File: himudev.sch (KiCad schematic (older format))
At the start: 2 parts

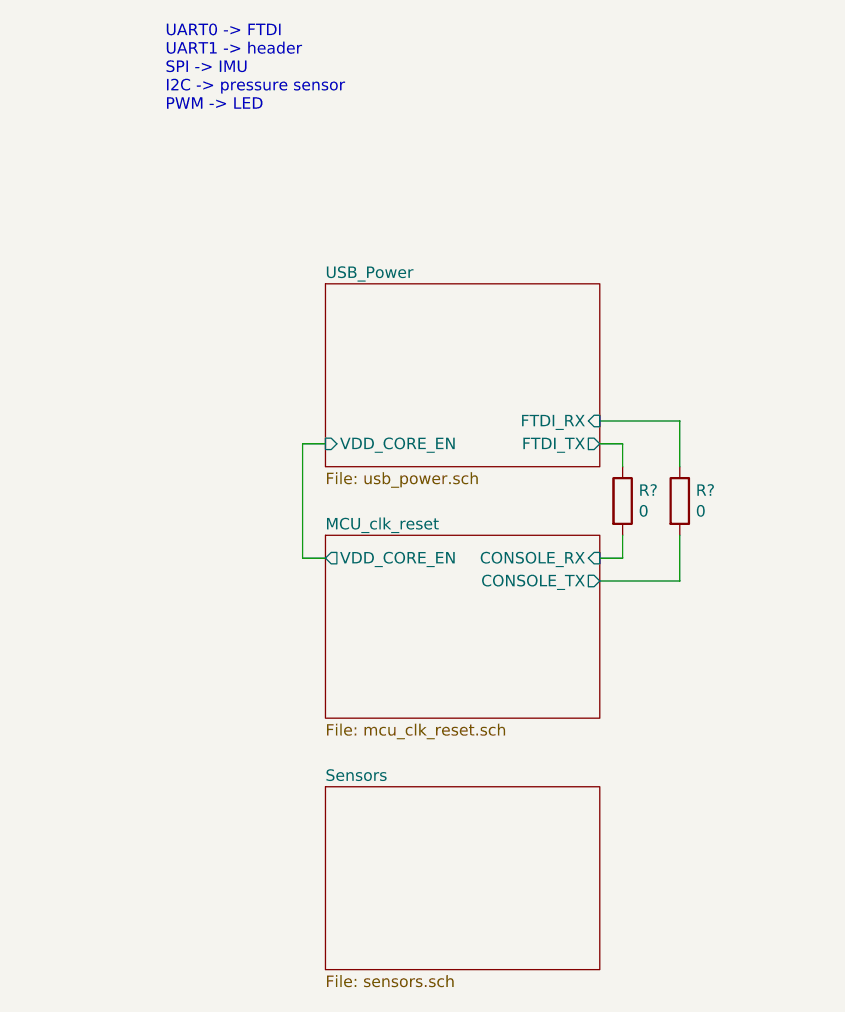
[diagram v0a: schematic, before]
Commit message: First full version of a schematic
This commit is a quicksave of completed but not reviewed schematic.
Added pressure sensor, finished IMU wiring, finished top-level
schematic, added pin header, placed LEDs and many others.
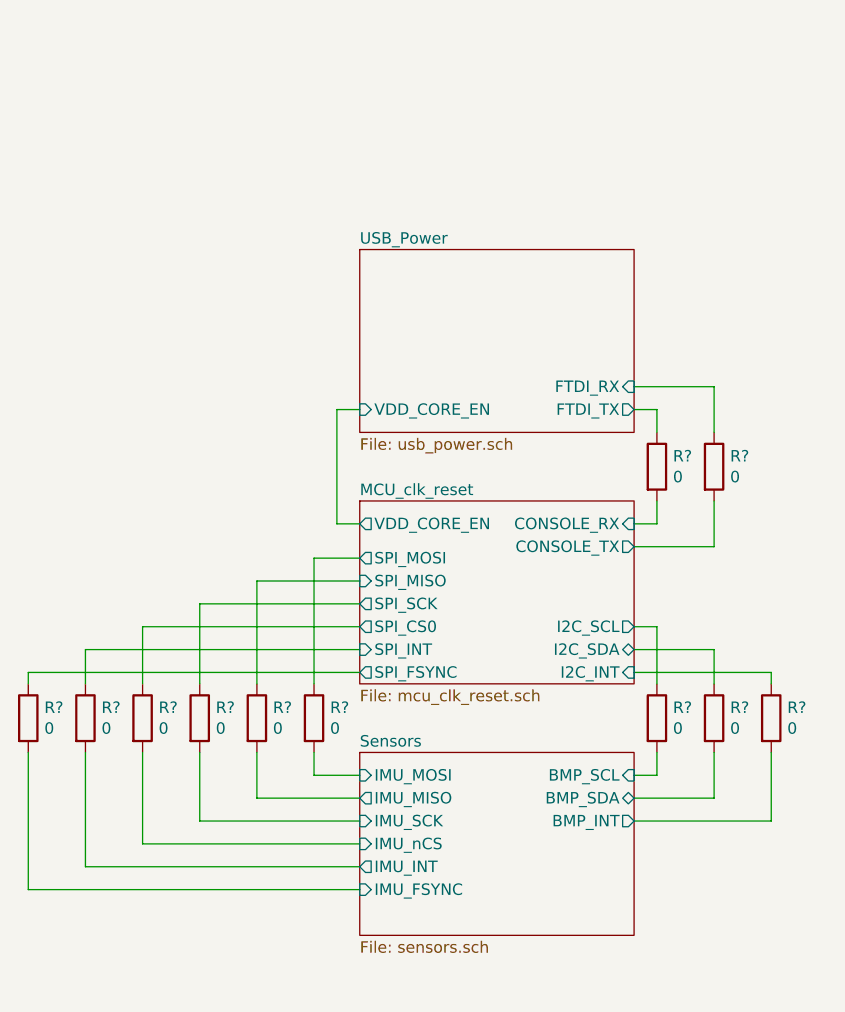
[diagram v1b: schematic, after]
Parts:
- added R? (x9): 0, symbol Device:R
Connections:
- new net MCU_clk_reset/I2C_INT: R?.1
- new net MCU_clk_reset/I2C_SCL: R?.1
- new net MCU_clk_reset/I2C_SDA: R?.1
- new net MCU_clk_reset/SPI_CS0: R?.1
- new net MCU_clk_reset/SPI_FSYNC: R?.1
- new net MCU_clk_reset/SPI_INT: R?.1
- new net MCU_clk_reset/SPI_MISO: R?.1
- new net MCU_clk_reset/SPI_MOSI: R?.1
- new net MCU_clk_reset/SPI_SCK: R?.1
- new net Sensors/BMP_INT: R?.2
- new net Sensors/BMP_SCL: R?.2
- new net Sensors/BMP_SDA: R?.2
- new net Sensors/IMU_FSYNC: R?.2
- new net Sensors/IMU_INT: R?.2
- new net Sensors/IMU_MISO: R?.2
- new net Sensors/IMU_MOSI: R?.2
- new net Sensors/IMU_SCK: R?.2
- new net Sensors/IMU_nCS: R?.2
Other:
- note removed: "UART0 -> FTDI\nUART1 -> header\nSPI -> IMU\nI2C -> pressure sensor\nPWM -> LED"
- moved on the sheet: R?

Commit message: Add ERC fixes, mostly PWR_FLAGs
Also, fixed MCP1726 symbol.
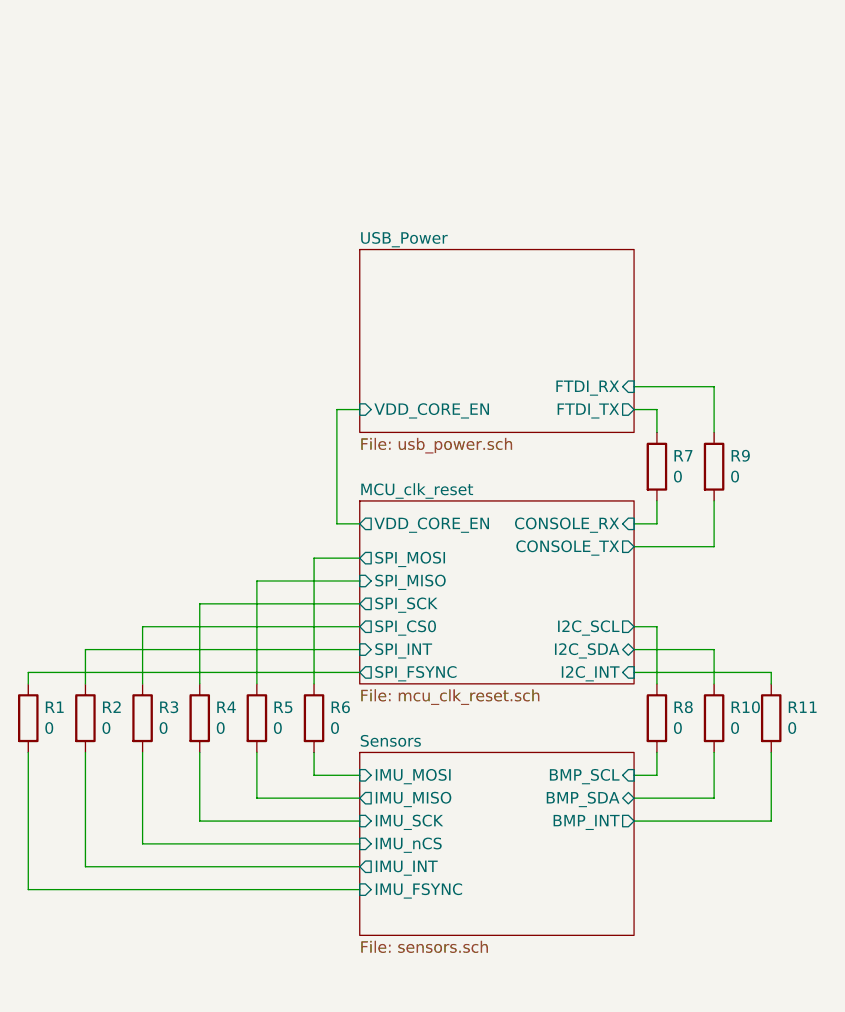
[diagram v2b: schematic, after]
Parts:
- gave numbers to parts that had none: 11
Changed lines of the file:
@@
 	6550 3650 6450 3650
 $Comp
-L Device:R R?
+L Device:R R7
 U 1 1 5E01A1E6
 P 6550 3400
-F 0 "R?" H 6620 3446 50  0000 L CNN
+F 0 "R7" H 6620 3446 50  0000 L CNN
 F 1 "0" H 6620 3355 50  0000 L CNN
 F 2 "" V 6480 3400 50  0001 C CNN
@@
 $EndComp
 $Comp
-L Device:R R?
+L Device:R R9
 U 1 1 5E01A80B
 P 6800 3400
-F 0 "R?" H 6870 3446 50  0000 L CNN
+F 0 "R9" H 6870 3446 50  0000 L CNN
 F 1 "0" H 6870 3355 50  0000 L CNN
 F 2 "" V 6730 3400 50  0001 C CNN
@@
 	6550 4750 6450 4750
 $Comp
-L Device:R R?
+L Device:R R8
 U 1 1 5EC7E790
 P 6550 4500
-F 0 "R?" H 6620 4546 50  0000 L CNN
+F 0 "R8" H 6620 4546 50  0000 L CNN
 F 1 "0" H 6620 4455 50  0000 L CNN
 F 2 "" V 6480 4500 50  0001 C CNN
@@
 $EndComp
 $Comp
-L Device:R R?
+L Device:R R10
 U 1 1 5EC7E796
 P 6800 4500
-F 0 "R?" H 6870 4546 50  0000 L CNN
+F 0 "R10" H 6870 4546 50  0000 L CNN
 F 1 "0" H 6870 4455 50  0000 L CNN
 F 2 "" V 6730 4500 50  0001 C CNN
@@
 	6450 4850 6800 4850
 $Comp
-L Device:R R?
+L Device:R R11
 U 1 1 5EC7F0AC
 P 7050 4500
-F 0 "R?" H 7120 4546 50  0000 L CNN
+F 0 "R11" H 7120 4546 50  0000 L CNN
 F 1 "0" H 7120 4455 50  0000 L CNN
 F 2 "" V 6980 4500 50  0001 C CNN
@@
 	6450 4950 7050 4950
 $Comp
-L Device:R R?
+L Device:R R4
 U 1 1 5ECADCAC
 P 4550 4500
-F 0 "R?" H 4620 4546 50  0000 L CNN
+F 0 "R4" H 4620 4546 50  0000 L CNN
 F 1 "0" H 4620 4455 50  0000 L CNN
 F 2 "" V 4480 4500 50  0001 C CNN
@@
 $EndComp
 $Comp
-L Device:R R?
+L Device:R R5
 U 1 1 5ECADCB2
 P 4800 4500
-F 0 "R?" H 4870 4546 50  0000 L CNN
+F 0 "R5" H 4870 4546 50  0000 L CNN
 F 1 "0" H 4870 4455 50  0000 L CNN
 F 2 "" V 4730 4500 50  0001 C CNN
@@
 $EndComp
 $Comp
-L Device:R R?
+L Device:R R6
 U 1 1 5ECADCB8
 P 5050 4500
-F 0 "R?" H 5120 4546 50  0000 L CNN
+F 0 "R6" H 5120 4546 50  0000 L CNN
 F 1 "0" H 5120 4455 50  0000 L CNN
 F 2 "" V 4980 4500 50  0001 C CNN
@@
 $EndComp
 $Comp
-L Device:R R?
+L Device:R R1
 U 1 1 5ECAE892
 P 3800 4500
-F 0 "R?" H 3870 4546 50  0000 L CNN
+F 0 "R1" H 3870 4546 50  0000 L CNN
 F 1 "0" H 3870 4455 50  0000 L CNN
 F 2 "" V 3730 4500 50  0001 C CNN
@@
 $EndComp
 $Comp
-L Device:R R?
+L Device:R R2
 U 1 1 5ECAE898
 P 4050 4500
-F 0 "R?" H 4120 4546 50  0000 L CNN
+F 0 "R2" H 4120 4546 50  0000 L CNN
 F 1 "0" H 4120 4455 50  0000 L CNN
 F 2 "" V 3980 4500 50  0001 C CNN
@@
 $EndComp
 $Comp
-L Device:R R?
+L Device:R R3
 U 1 1 5ECAE89E
 P 4300 4500
-F 0 "R?" H 4370 4546 50  0000 L CNN
+F 0 "R3" H 4370 4546 50  0000 L CNN
 F 1 "0" H 4370 4455 50  0000 L CNN
 F 2 "" V 4230 4500 50  0001 C CNN

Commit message: Assigned footprints, generated netlist
I can already see some footprints issues. Eg. the switches have to be
changed to the SMT version. There are some silkscreen issues in custom
oscillator footprints. Otherwise looks promising :)
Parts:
- R1, R10, R11, R2, R3, R4, R5, R6, R7, R8, R9: footprint (none) -> Resistor_SMD:R_0805_2012Metric_Pad1.15x1.40mm_HandSolder
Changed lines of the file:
@@
 F 0 "R7" H 6620 3446 50  0000 L CNN
 F 1 "0" H 6620 3355 50  0000 L CNN
-F 2 "" V 6480 3400 50  0001 C CNN
+F 2 "Resistor_SMD:R_0805_2012Metric_Pad1.15x1.40mm_HandSolder" V 6480 3400 50  0001 C CNN
 F 3 "~" H 6550 3400 50  0001 C CNN
 	1    6550 3400
@@
 F 0 "R9" H 6870 3446 50  0000 L CNN
 F 1 "0" H 6870 3355 50  0000 L CNN
-F 2 "" V 6730 3400 50  0001 C CNN
+F 2 "Resistor_SMD:R_0805_2012Metric_Pad1.15x1.40mm_HandSolder" V 6730 3400 50  0001 C CNN
 F 3 "~" H 6800 3400 50  0001 C CNN
 	1    6800 3400
@@
 F 0 "R8" H 6620 4546 50  0000 L CNN
 F 1 "0" H 6620 4455 50  0000 L CNN
-F 2 "" V 6480 4500 50  0001 C CNN
+F 2 "Resistor_SMD:R_0805_2012Metric_Pad1.15x1.40mm_HandSolder" V 6480 4500 50  0001 C CNN
 F 3 "~" H 6550 4500 50  0001 C CNN
 	1    6550 4500
@@
 F 0 "R10" H 6870 4546 50  0000 L CNN
 F 1 "0" H 6870 4455 50  0000 L CNN
-F 2 "" V 6730 4500 50  0001 C CNN
+F 2 "Resistor_SMD:R_0805_2012Metric_Pad1.15x1.40mm_HandSolder" V 6730 4500 50  0001 C CNN
 F 3 "~" H 6800 4500 50  0001 C CNN
 	1    6800 4500
@@
 F 0 "R11" H 7120 4546 50  0000 L CNN
 F 1 "0" H 7120 4455 50  0000 L CNN
-F 2 "" V 6980 4500 50  0001 C CNN
+F 2 "Resistor_SMD:R_0805_2012Metric_Pad1.15x1.40mm_HandSolder" V 6980 4500 50  0001 C CNN
 F 3 "~" H 7050 4500 50  0001 C CNN
 	1    7050 4500
@@
 F 0 "R4" H 4620 4546 50  0000 L CNN
 F 1 "0" H 4620 4455 50  0000 L CNN
-F 2 "" V 4480 4500 50  0001 C CNN
+F 2 "Resistor_SMD:R_0805_2012Metric_Pad1.15x1.40mm_HandSolder" V 4480 4500 50  0001 C CNN
 F 3 "~" H 4550 4500 50  0001 C CNN
 	1    4550 4500
@@
 F 0 "R5" H 4870 4546 50  0000 L CNN
 F 1 "0" H 4870 4455 50  0000 L CNN
-F 2 "" V 4730 4500 50  0001 C CNN
+F 2 "Resistor_SMD:R_0805_2012Metric_Pad1.15x1.40mm_HandSolder" V 4730 4500 50  0001 C CNN
 F 3 "~" H 4800 4500 50  0001 C CNN
 	1    4800 4500
@@
 F 0 "R6" H 5120 4546 50  0000 L CNN
 F 1 "0" H 5120 4455 50  0000 L CNN
-F 2 "" V 4980 4500 50  0001 C CNN
+F 2 "Resistor_SMD:R_0805_2012Metric_Pad1.15x1.40mm_HandSolder" V 4980 4500 50  0001 C CNN
 F 3 "~" H 5050 4500 50  0001 C CNN
 	1    5050 4500
@@
 F 0 "R1" H 3870 4546 50  0000 L CNN
 F 1 "0" H 3870 4455 50  0000 L CNN
-F 2 "" V 3730 4500 50  0001 C CNN
+F 2 "Resistor_SMD:R_0805_2012Metric_Pad1.15x1.40mm_HandSolder" V 3730 4500 50  0001 C CNN
 F 3 "~" H 3800 4500 50  0001 C CNN
 	1    3800 4500
@@
 F 0 "R2" H 4120 4546 50  0000 L CNN
 F 1 "0" H 4120 4455 50  0000 L CNN
-F 2 "" V 3980 4500 50  0001 C CNN
+F 2 "Resistor_SMD:R_0805_2012Metric_Pad1.15x1.40mm_HandSolder" V 3980 4500 50  0001 C CNN
 F 3 "~" H 4050 4500 50  0001 C CNN
 	1    4050 4500
@@
 F 0 "R3" H 4370 4546 50  0000 L CNN
 F 1 "0" H 4370 4455 50  0000 L CNN
-F 2 "" V 4230 4500 50  0001 C CNN
+F 2 "Resistor_SMD:R_0805_2012Metric_Pad1.15x1.40mm_HandSolder" V 4230 4500 50  0001 C CNN
 F 3 "~" H 4300 4500 50  0001 C CNN
 	1    4300 4500

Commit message: Use 0603 components, on both sides, route header
This decision was due to the current placement overcrowded and to the
fact that successful routing on one side was uncertain.
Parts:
- R1, R10, R11, R2, R3, R4, R5, R6, R7, R8, R9: footprint Resistor_SMD:R_0805_2012Metric_Pad1.15x1.40mm_HandSolder -> Resistor_SMD:R_0603_1608Metric_Pad1.05x0.95mm_HandSolder
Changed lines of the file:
@@
 F 0 "R7" H 6620 3446 50  0000 L CNN
 F 1 "0" H 6620 3355 50  0000 L CNN
-F 2 "Resistor_SMD:R_0805_2012Metric_Pad1.15x1.40mm_HandSolder" V 6480 3400 50  0001 C CNN
+F 2 "Resistor_SMD:R_0603_1608Metric_Pad1.05x0.95mm_HandSolder" V 6480 3400 50  0001 C CNN
 F 3 "~" H 6550 3400 50  0001 C CNN
 	1    6550 3400
@@
 F 0 "R9" H 6870 3446 50  0000 L CNN
 F 1 "0" H 6870 3355 50  0000 L CNN
-F 2 "Resistor_SMD:R_0805_2012Metric_Pad1.15x1.40mm_HandSolder" V 6730 3400 50  0001 C CNN
+F 2 "Resistor_SMD:R_0603_1608Metric_Pad1.05x0.95mm_HandSolder" V 6730 3400 50  0001 C CNN
 F 3 "~" H 6800 3400 50  0001 C CNN
 	1    6800 3400
@@
 F 0 "R8" H 6620 4546 50  0000 L CNN
 F 1 "0" H 6620 4455 50  0000 L CNN
-F 2 "Resistor_SMD:R_0805_2012Metric_Pad1.15x1.40mm_HandSolder" V 6480 4500 50  0001 C CNN
+F 2 "Resistor_SMD:R_0603_1608Metric_Pad1.05x0.95mm_HandSolder" V 6480 4500 50  0001 C CNN
 F 3 "~" H 6550 4500 50  0001 C CNN
 	1    6550 4500
@@
 F 0 "R10" H 6870 4546 50  0000 L CNN
 F 1 "0" H 6870 4455 50  0000 L CNN
-F 2 "Resistor_SMD:R_0805_2012Metric_Pad1.15x1.40mm_HandSolder" V 6730 4500 50  0001 C CNN
+F 2 "Resistor_SMD:R_0603_1608Metric_Pad1.05x0.95mm_HandSolder" V 6730 4500 50  0001 C CNN
 F 3 "~" H 6800 4500 50  0001 C CNN
 	1    6800 4500
@@
 F 0 "R11" H 7120 4546 50  0000 L CNN
 F 1 "0" H 7120 4455 50  0000 L CNN
-F 2 "Resistor_SMD:R_0805_2012Metric_Pad1.15x1.40mm_HandSolder" V 6980 4500 50  0001 C CNN
+F 2 "Resistor_SMD:R_0603_1608Metric_Pad1.05x0.95mm_HandSolder" V 6980 4500 50  0001 C CNN
 F 3 "~" H 7050 4500 50  0001 C CNN
 	1    7050 4500
@@
 F 0 "R4" H 4620 4546 50  0000 L CNN
 F 1 "0" H 4620 4455 50  0000 L CNN
-F 2 "Resistor_SMD:R_0805_2012Metric_Pad1.15x1.40mm_HandSolder" V 4480 4500 50  0001 C CNN
+F 2 "Resistor_SMD:R_0603_1608Metric_Pad1.05x0.95mm_HandSolder" V 4480 4500 50  0001 C CNN
 F 3 "~" H 4550 4500 50  0001 C CNN
 	1    4550 4500
@@
 F 0 "R5" H 4870 4546 50  0000 L CNN
 F 1 "0" H 4870 4455 50  0000 L CNN
-F 2 "Resistor_SMD:R_0805_2012Metric_Pad1.15x1.40mm_HandSolder" V 4730 4500 50  0001 C CNN
+F 2 "Resistor_SMD:R_0603_1608Metric_Pad1.05x0.95mm_HandSolder" V 4730 4500 50  0001 C CNN
 F 3 "~" H 4800 4500 50  0001 C CNN
 	1    4800 4500
@@
 F 0 "R6" H 5120 4546 50  0000 L CNN
 F 1 "0" H 5120 4455 50  0000 L CNN
-F 2 "Resistor_SMD:R_0805_2012Metric_Pad1.15x1.40mm_HandSolder" V 4980 4500 50  0001 C CNN
+F 2 "Resistor_SMD:R_0603_1608Metric_Pad1.05x0.95mm_HandSolder" V 4980 4500 50  0001 C CNN
 F 3 "~" H 5050 4500 50  0001 C CNN
 	1    5050 4500
@@
 F 0 "R1" H 3870 4546 50  0000 L CNN
 F 1 "0" H 3870 4455 50  0000 L CNN
-F 2 "Resistor_SMD:R_0805_2012Metric_Pad1.15x1.40mm_HandSolder" V 3730 4500 50  0001 C CNN
+F 2 "Resistor_SMD:R_0603_1608Metric_Pad1.05x0.95mm_HandSolder" V 3730 4500 50  0001 C CNN
 F 3 "~" H 3800 4500 50  0001 C CNN
 	1    3800 4500
@@
 F 0 "R2" H 4120 4546 50  0000 L CNN
 F 1 "0" H 4120 4455 50  0000 L CNN
-F 2 "Resistor_SMD:R_0805_2012Metric_Pad1.15x1.40mm_HandSolder" V 3980 4500 50  0001 C CNN
+F 2 "Resistor_SMD:R_0603_1608Metric_Pad1.05x0.95mm_HandSolder" V 3980 4500 50  0001 C CNN
 F 3 "~" H 4050 4500 50  0001 C CNN
 	1    4050 4500
@@
 F 0 "R3" H 4370 4546 50  0000 L CNN
 F 1 "0" H 4370 4455 50  0000 L CNN
-F 2 "Resistor_SMD:R_0805_2012Metric_Pad1.15x1.40mm_HandSolder" V 4230 4500 50  0001 C CNN
+F 2 "Resistor_SMD:R_0603_1608Metric_Pad1.05x0.95mm_HandSolder" V 4230 4500 50  0001 C CNN
 F 3 "~" H 4300 4500 50  0001 C CNN
 	1    4300 4500
